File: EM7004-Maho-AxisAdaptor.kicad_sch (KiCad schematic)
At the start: 6 parts, among them J1 1830498, J2 1830498, J3 D-SUB-DR-15PCM-CB, J4 D-SUB-DR-15PCM-CB, J5 DMR-9S, J6 XY2500R-D-5.08-2P

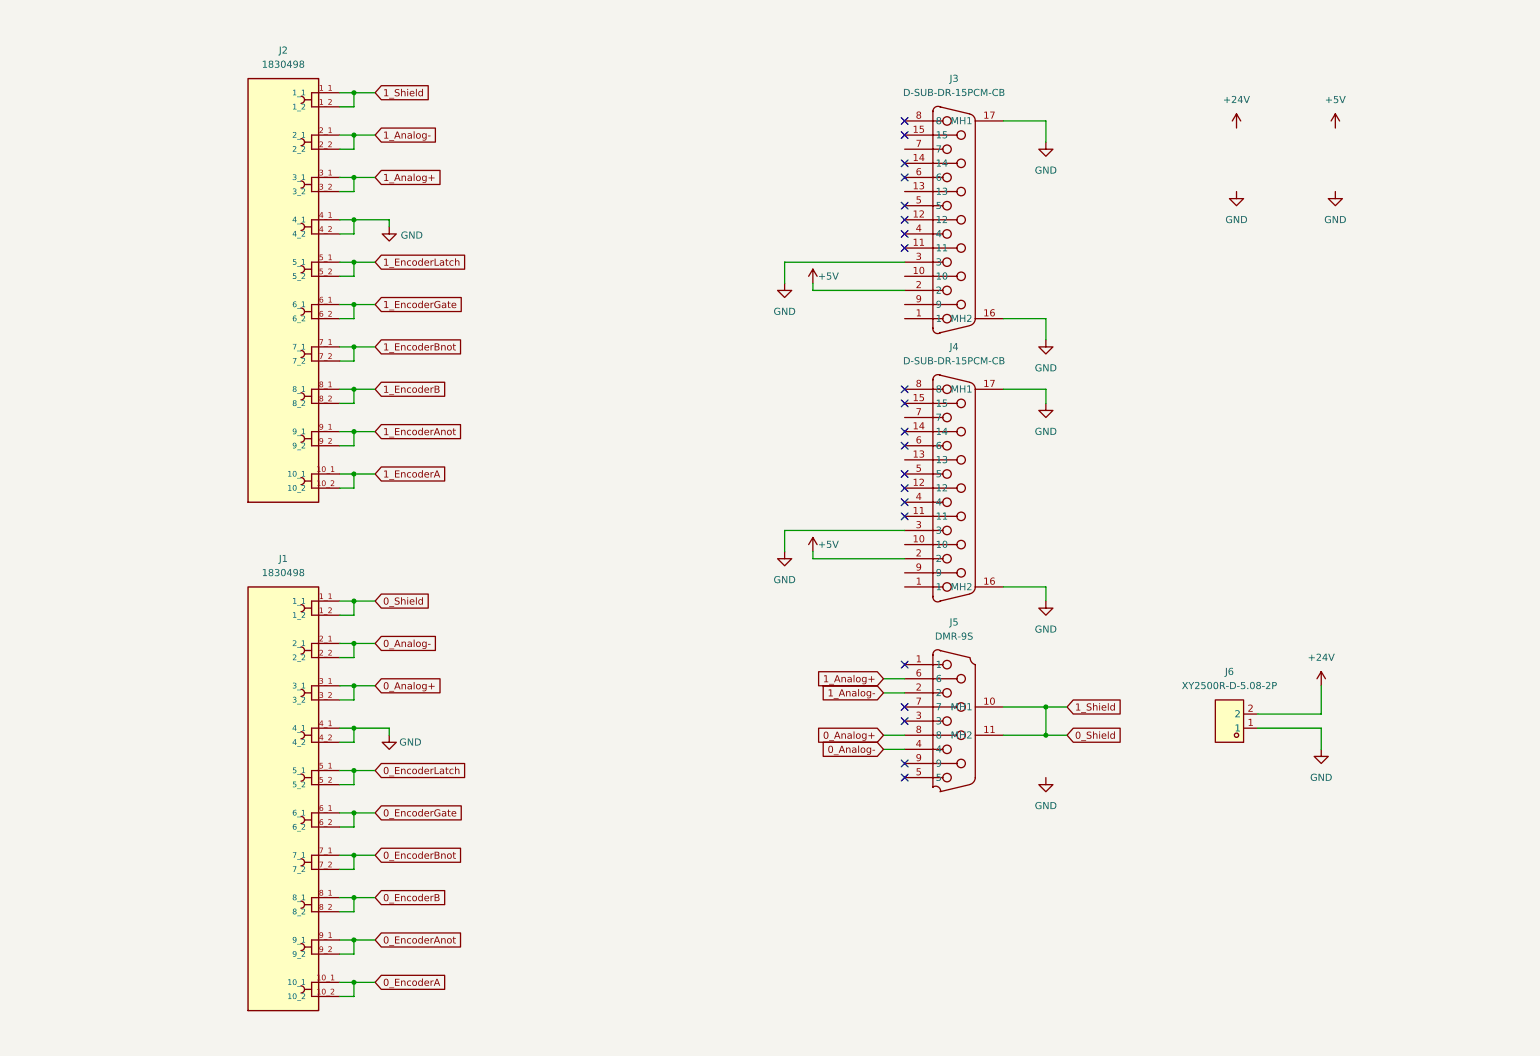
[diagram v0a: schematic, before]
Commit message: added 5V regulator
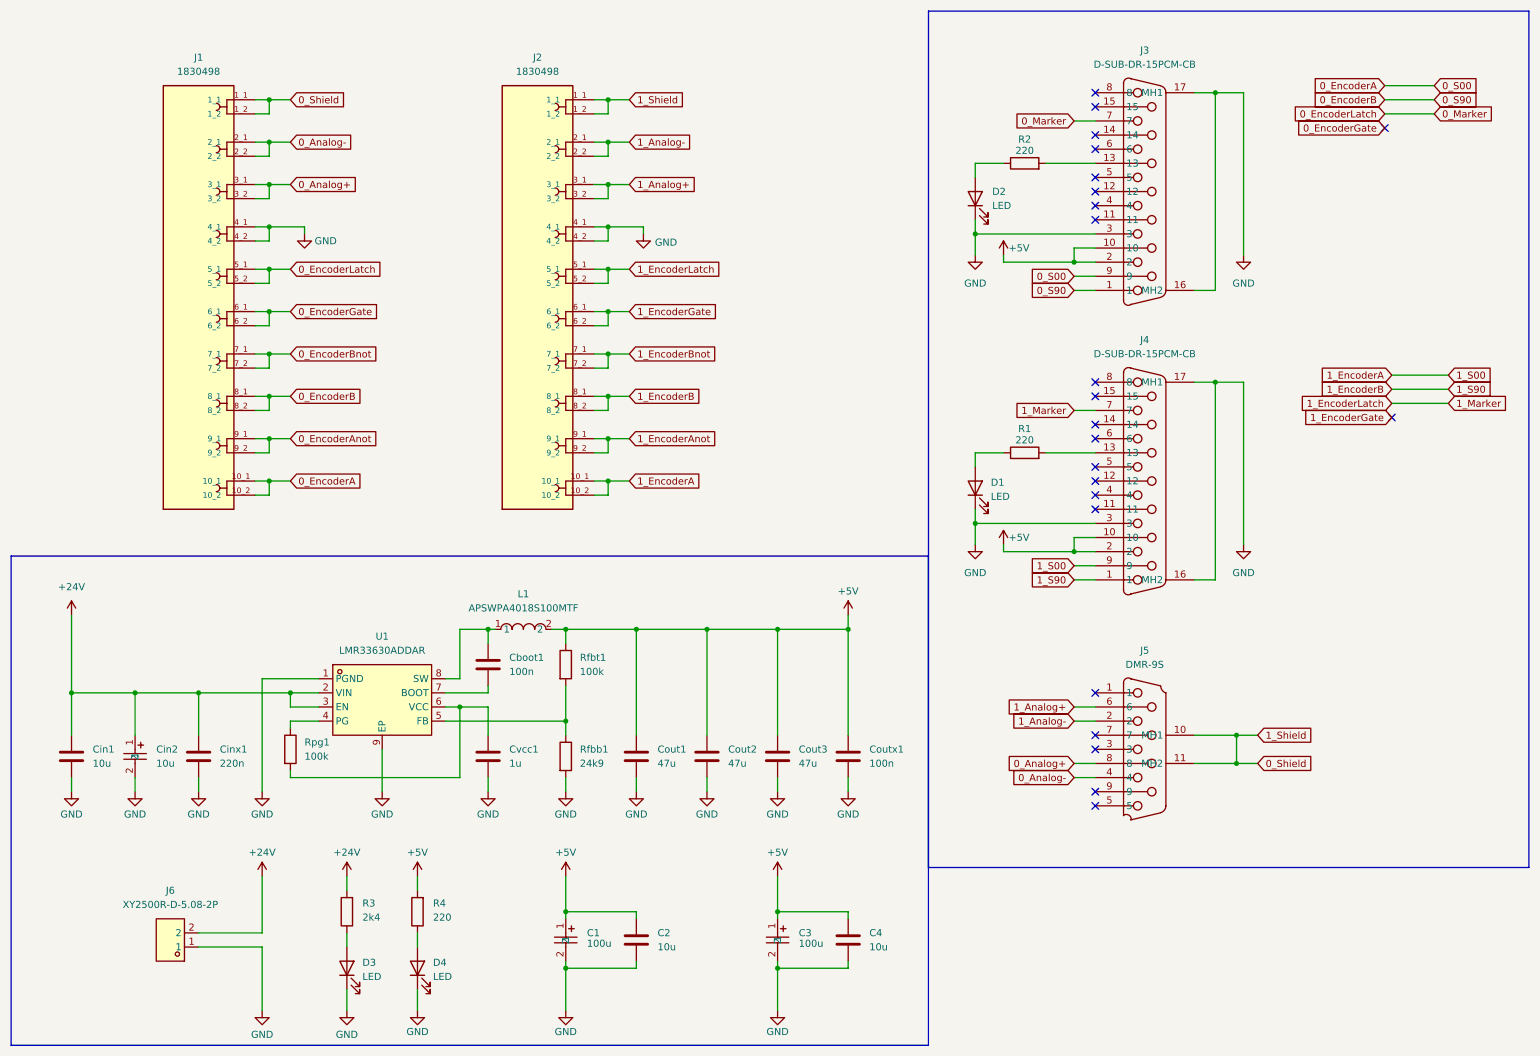
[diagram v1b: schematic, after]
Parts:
- added C1, C3: 100u, easyeda2kicad:CASE-D_7343, symbol easyeda2kicad:TAJD157K016RNJ
- added C2, C4, Cin1: 10u, Capacitor_SMD:C_1210_3225Metric, symbol Device:C
- added Cboot1: 100n, Capacitor_SMD:C_0603_1608Metric, symbol Device:C
- added Cin2: 10u, easyeda2kicad:CAP-SMD_L7.3-W4.3-R-RD, symbol easyeda2kicad:T491D106K050AT
- added Cinx1: 220n, Capacitor_SMD:C_0805_2012Metric, symbol Device:C
- added Cout1, Cout2, Cout3: 47u, Capacitor_SMD:C_1206_3216Metric, symbol Device:C
- added Coutx1: 100n, Capacitor_SMD:C_0805_2012Metric, symbol Device:C
- added Cvcc1: 1u, Capacitor_SMD:C_0603_1608Metric, symbol Device:C
- added D1, D2, D3, D4: LED, LED_SMD:LED_0603_1608Metric, symbol Device:LED
- added L1: APSWPA4018S100MTF, easyeda2kicad:IND-SMD_L4.0-W4.0, symbol easyeda2kicad:APSWPA4018S100MTF
- added R1, R2, R4: 220, Resistor_SMD:R_0603_1608Metric, symbol Device:R
- added R3: 2k4, Resistor_SMD:R_0603_1608Metric, symbol Device:R
- added Rfbb1: 24k9, Capacitor_SMD:C_0603_1608Metric, symbol Device:R
- added Rfbt1, Rpg1: 100k, Capacitor_SMD:C_0603_1608Metric, symbol Device:R
- added U1: LMR33630ADDAR, easyeda2kicad:ESOP-8_L4.9-W3.9-P1.27-LS6.0-TL-EP, symbol easyeda2kicad:LMR33630ADDAR
- renumbered J4 to J3, J3 to J4
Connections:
- net +24V: now also Cin1.1, Cin2.1, Cinx1.1, R3.2, U1.2 (VIN), U1.3 (EN)
- net +5V: now also J3.10, J4.10, C1.1, C2.1, C3.1, C4.1, Cout1.1, Cout2.1, Cout3.1, Coutx1.1, L1.2, R4.2, Rfbt1.1
- net 0_EncoderA: now also J3.9
- net 0_EncoderB: now also J3.1
- net 0_EncoderLatch: now also J3.7
- net 1_EncoderA: now also J4.9
- net 1_EncoderB: now also J4.1
- net 1_EncoderLatch: now also J4.7
- net GND: now also C1.2, C2.2, C3.2, C4.2, Cin1.2, Cin2.2, Cinx1.2, Cout1.2, Cout2.2, Cout3.2, Coutx1.2, Cvcc1.2, D1.1 (K), D2.1 (K), D3.1 (K), D4.1 (K), Rfbb1.2, U1.1 (PGND), U1.9 (EP)
- net at J3.13: now also R2.2
- net at J4.13: now also R1.2
- new net: Cboot1.1, L1.1, U1.8 (SW)
- new net: Rpg1.1, U1.4 (PG)
- new net: Cvcc1.1, Rpg1.2, U1.6 (VCC)
- new net: D1.2 (A), R1.1
- new net: D4.2 (A), R4.1
- new net: D2.2 (A), R2.1
- new net: D3.2 (A), R3.1
- new net: Rfbb1.1, Rfbt1.2, U1.5 (FB)
- new net: Cboot1.2, U1.7 (BOOT)
- no-connect marks 21 -> 23
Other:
- title: (none) -> EM7004-Maho-Philips-432
- moved on the sheet: J1, J2, J3, J4, J5, J6

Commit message: finalized v0.9.2 design
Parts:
- added J7: S2B-XH-A-1 (LF)(SN), easyeda2kicad:CONN-TH_S2B-XH-A-1-LF-SN, symbol Connector:Conn_01x02_Pin
- added R5: 0R, Resistor_SMD:R_0603_1608Metric, symbol Device:R
- R1, R2, R4: value 220 -> 680
- R3: value 2k4 -> 4k7
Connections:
- net +5V: now also J7.1 (Pin_1)
- net 0_Shield: now also R5.1
- net GND: now also J7.2 (Pin_2), R5.2
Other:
- moved on the sheet: C2, D3, D4, J6, R3, R4

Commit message: last commit before archiving
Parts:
- added JP0, JP1: Latch/Gate-Marker, Jumper:SolderJumper-3_P1.3mm_Bridged12_Pad1.0x1.5mm, symbol Jumper:SolderJumper_3_Bridged12
- renumbered J1 to J00, J3 to J01, J2 to J10, J4 to J11, J5 to J2, J6 to J3, J7 to J4
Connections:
- net 0_EncoderGate: now also JP0.3 (B)
- net 0_EncoderLatch: now also JP0.1 (A); no longer J01.7
- net 1_EncoderGate: now also JP1.3 (B)
- net 1_EncoderLatch: now also JP1.1 (A); no longer J11.7
- new net 0_Marker: J01.7, JP0.2 (C)
- new net 1_Marker: J11.7, JP1.2 (C)
- no-connect marks 23 -> 21
